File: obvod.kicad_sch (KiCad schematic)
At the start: 1 part

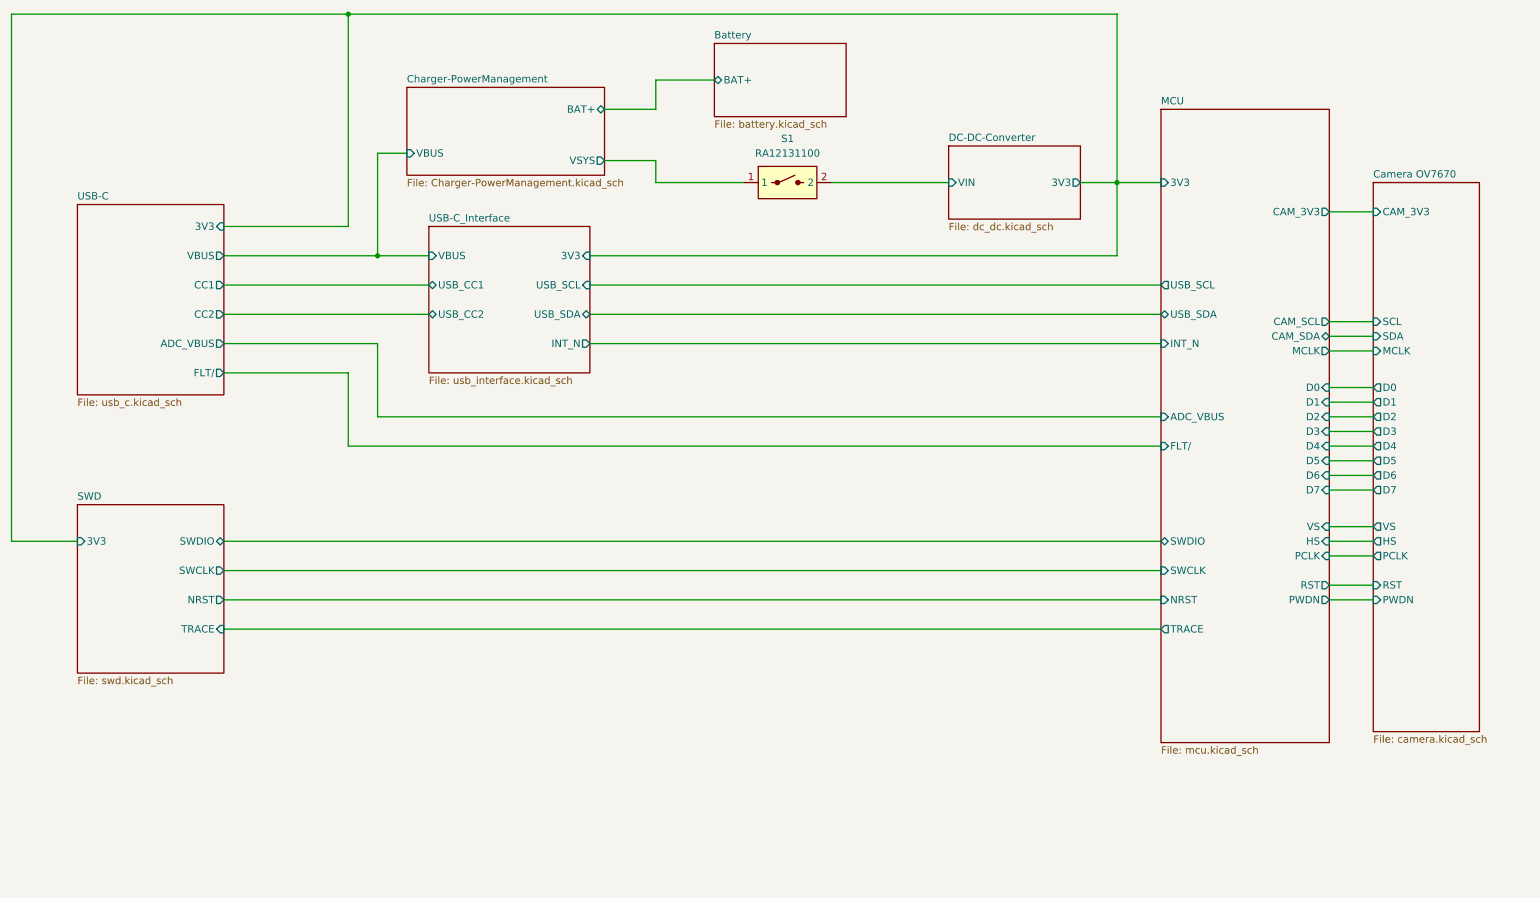
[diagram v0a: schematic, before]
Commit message: USB-B micro added
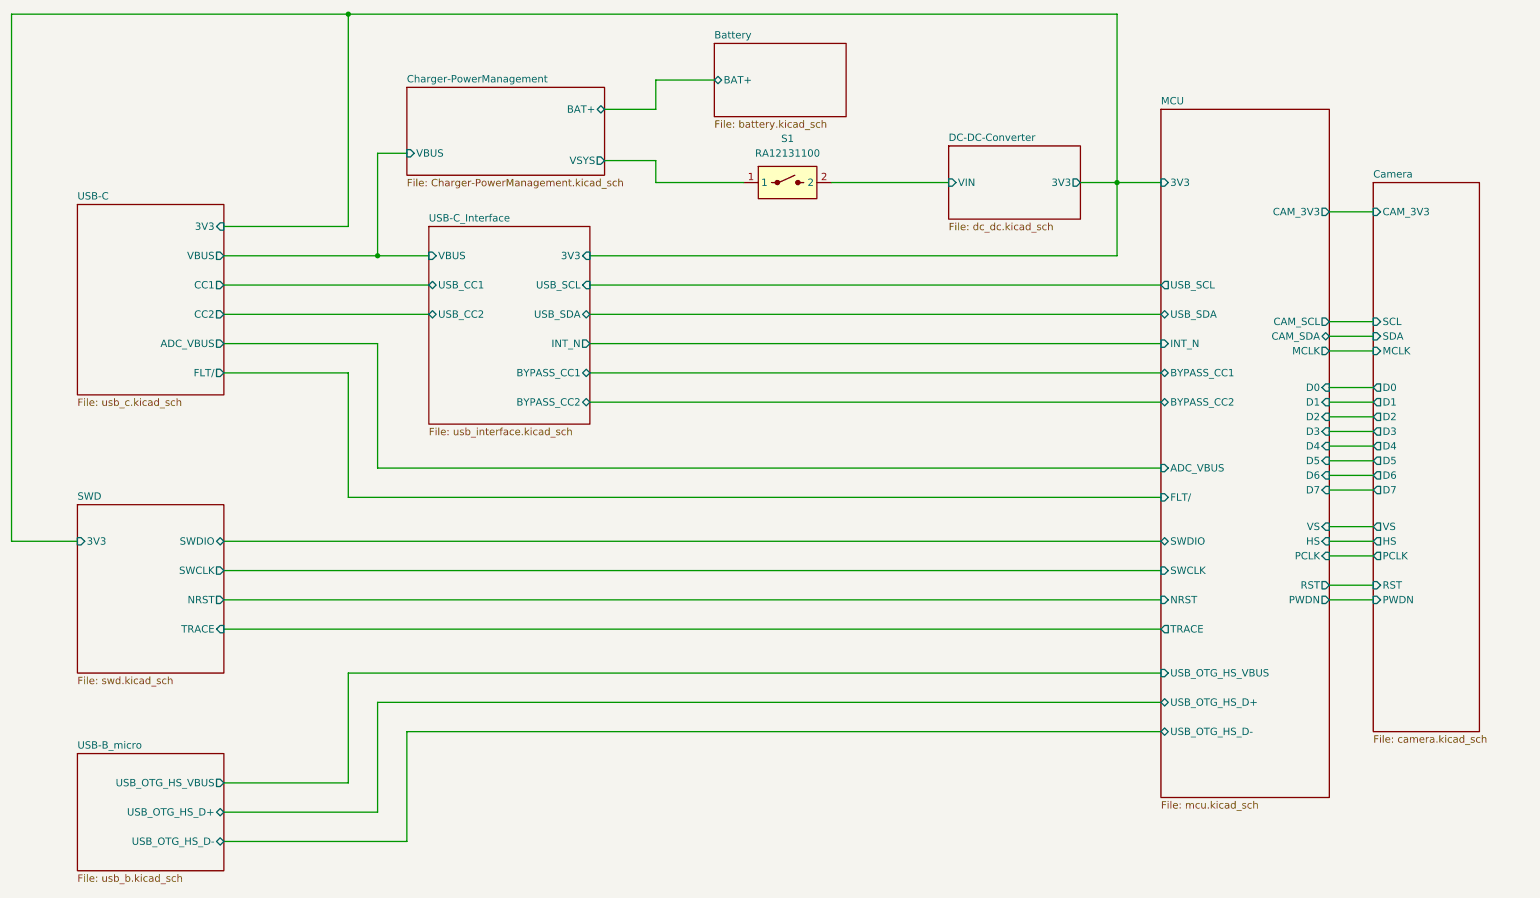
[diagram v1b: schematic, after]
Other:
- sheet Camera OV7670 renamed Camera
- added sheet USB-B_micro (usb_b.kicad_sch)
- sheet MCU ports: added BYPASS_CC1, BYPASS_CC2, USB_OTG_HS_D+, USB_OTG_HS_D-, USB_OTG_HS_VBUS; removed none
- sheet USB-C_Interface ports: added BYPASS_CC1, BYPASS_CC2; removed none
